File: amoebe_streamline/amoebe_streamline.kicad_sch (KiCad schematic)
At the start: 0 parts

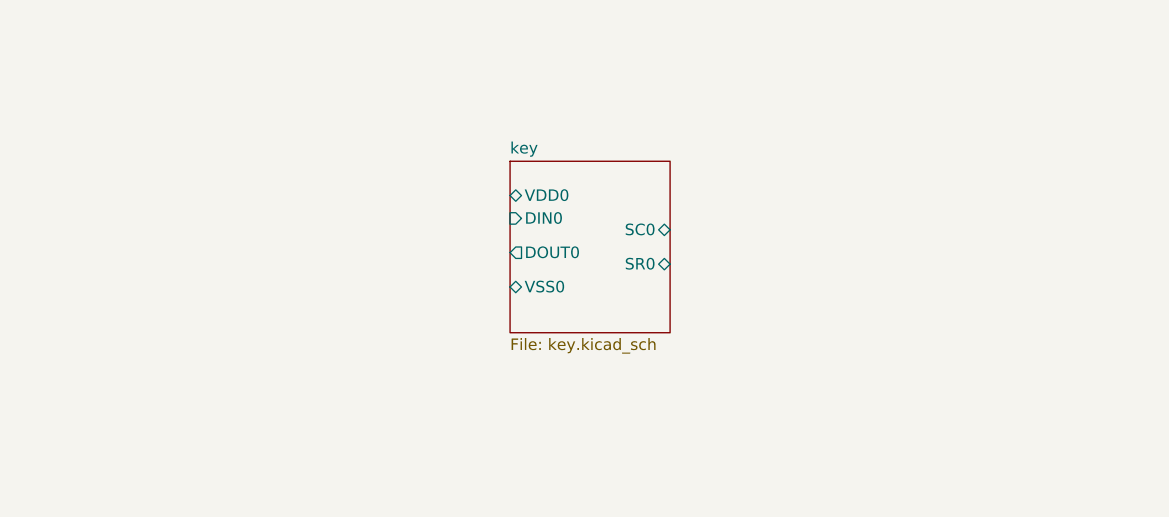
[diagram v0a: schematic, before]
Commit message: Finished schematic and routed traces
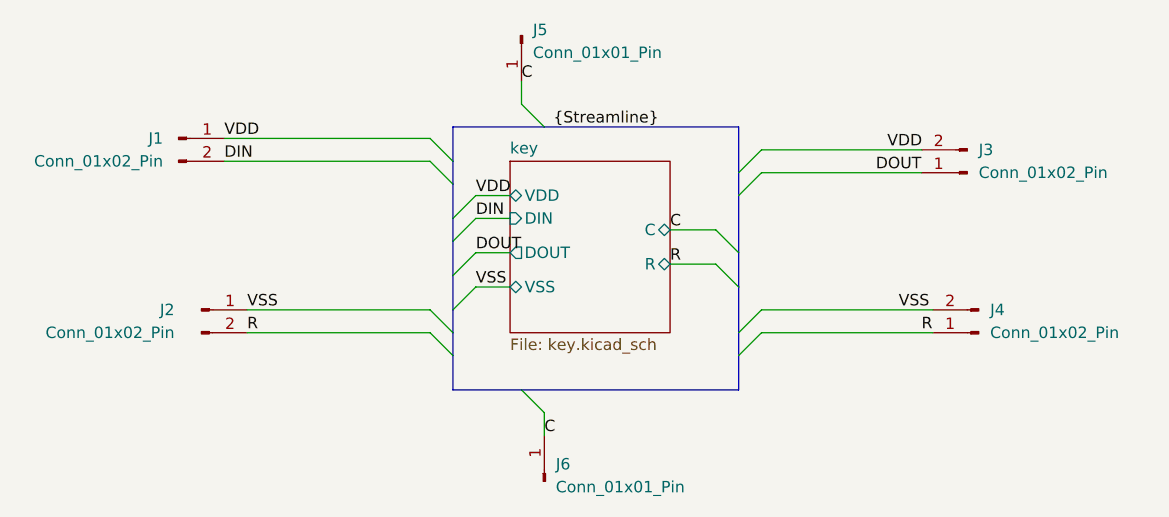
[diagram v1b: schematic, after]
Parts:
- added J1, J2, J3, J4: Conn_01x02_Pin, Connector_Molex:Molex_PicoBlade_53048-0210_1x02_P1.25mm_Horizontal, symbol Connector:Conn_01x02_Pin
- added J5, J6: Conn_01x01_Pin, Connector_PinHeader_1.00mm:PinHeader_1x01_P1.00mm_Horizontal, symbol Connector:Conn_01x01_Pin
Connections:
- new net C: J5.1 (Pin_1), J6.1 (Pin_1)
- new net DIN: J1.2 (Pin_2)
- new net DOUT: J3.1 (Pin_1)
- new net R: J2.2 (Pin_2), J4.1 (Pin_1)
- new net VDD: J1.1 (Pin_1), J3.2 (Pin_2)
- new net VSS: J2.1 (Pin_1), J4.2 (Pin_2)
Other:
- sheet key ports: added C, DIN, DOUT, R, VDD, VSS; removed DIN0, DOUT0, SC0, SR0, VDD0, VSS0

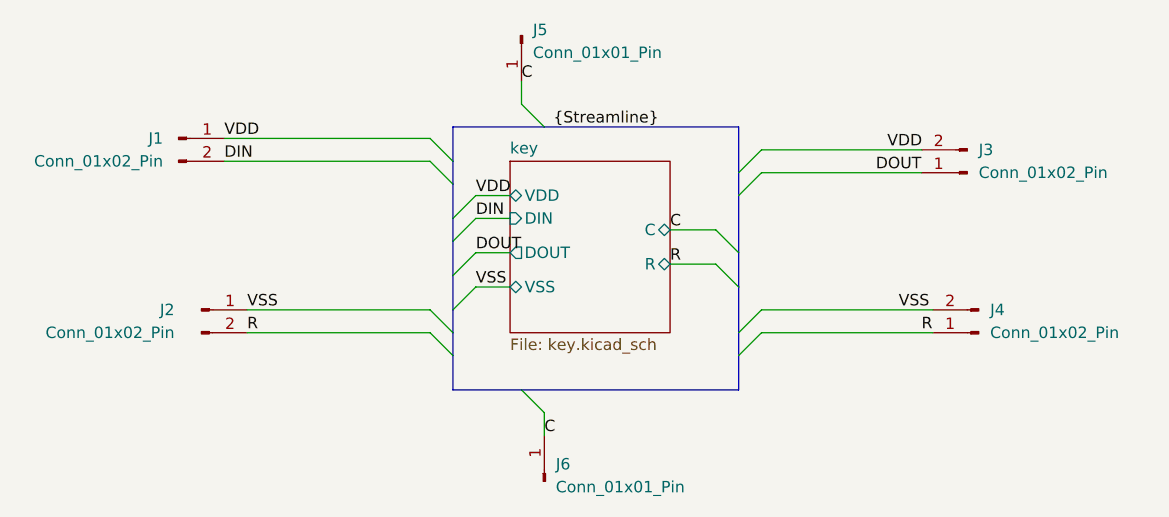
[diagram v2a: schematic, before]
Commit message: version 1.2 with additional ground pins
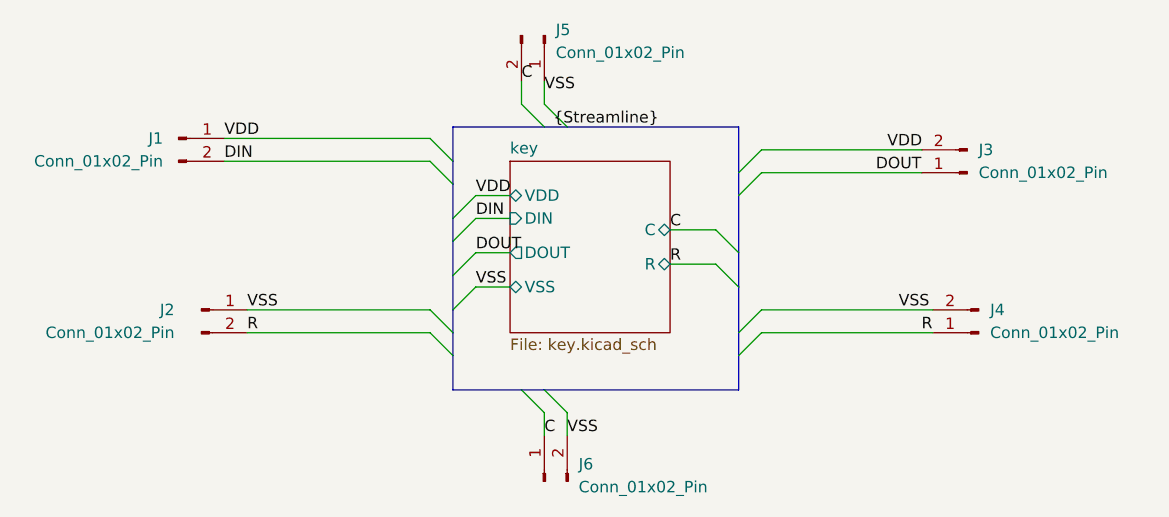
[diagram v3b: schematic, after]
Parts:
- removed J5, J6: Conn_01x01_Pin, Connector_PinHeader_1.00mm:PinHeader_1x01_P1.00mm_Horizontal, symbol Connector:Conn_01x01_Pin
- added J5, J6: Conn_01x02_Pin, Connector_PinHeader_1.00mm:PinHeader_1x02_P1.00mm_Horizontal, symbol Connector:Conn_01x02_Pin
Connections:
- net C: now also J5.2 (Pin_2), J6.1 (Pin_1)
- net VSS: now also J5.1 (Pin_1), J6.2 (Pin_2)
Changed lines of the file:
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@@
 (kicad_sch (version 20230121) (generator eeschema)
   (paper "A4")
-  (bus_alias "Streamline" (members "VDD" "VSS" "R" "C" "DATA"))
+  (bus_alias "Streamline" (members "VDD" "VSS" "R" "C" "DIN" "DOUT"))
   (bus_entry (at 132.08 78.74) (size -2.54 -2.54)
     (stroke (width 0) (type default))
@@
     (stroke (width 0) (type default))
   )
+  (bus_entry (at 144.78 72.39) (size -2.54 -2.54)
+    (stroke (width 0) (type default))
+  )
   (bus_entry (at 132.08 97.79) (size -2.54 -2.54)
     (stroke (width 0) (type default))
@@
     (stroke (width 0) (type default))
   )
+  (bus_entry (at 142.24 101.6) (size 2.54 2.54)
+    (stroke (width 0) (type default))
+  )
   (bus_entry (at 163.83 90.17) (size -2.54 -2.54)
     (stroke (width 0) (type default))
@@
     (stroke (width 0) (type default))
   )
+  (wire (pts (xy 144.78 104.14) (xy 144.78 106.68))
+    (stroke (width 0) (type default))
+  )
   (wire (pts (xy 161.29 87.63) (xy 156.21 87.63))
     (stroke (width 0) (type default))
@@
     (stroke (width 0) (type default))
   )
+  (bus (pts (xy 144.78 72.39) (xy 163.83 72.39))
+    (stroke (width 0) (type default))
+  )
   (bus (pts (xy 163.83 97.79) (xy 163.83 101.6))
     (stroke (width 0) (type default))
@@
     (stroke (width 0) (type default))
   )
+  (wire (pts (xy 142.24 67.31) (xy 142.24 69.85))
+    (stroke (width 0) (type default))
+  )
   (wire (pts (xy 139.7 69.85) (xy 139.7 67.31))
     (stroke (width 0) (type default))
@@
     (stroke (width 0) (type default))
   )
-  (bus (pts (xy 142.24 72.39) (xy 163.83 72.39))
+  (bus (pts (xy 142.24 72.39) (xy 144.78 72.39))
     (stroke (width 0) (type default))
   )
@@
     (stroke (width 0) (type default))
   )
-  (bus (pts (xy 139.7 101.6) (xy 163.83 101.6))
+  (bus (pts (xy 139.7 101.6) (xy 142.24 101.6))
     (stroke (width 0) (type default))
   )
   (bus (pts (xy 132.08 85.09) (xy 132.08 88.9))
+    (stroke (width 0) (type default))
+  )
+  (bus (pts (xy 142.24 101.6) (xy 163.83 101.6))
     (stroke (width 0) (type default))
   )
@@
     (effects (font (size 1.27 1.27)) (justify left bottom))
   )
+  (label "VSS" (at 144.78 106.68 0)
+    (effects (font (size 1.27 1.27)) (justify left bottom))
+  )
   (label "R" (at 156.21 87.63 0) (fields_autoplaced)
+    (effects (font (size 1.27 1.27)) (justify left bottom))
+  )
+  (label "VSS" (at 142.24 68.58 0)
     (effects (font (size 1.27 1.27)) (justify left bottom))
   )
@@
     )
   )
-  (symbol (lib_id "Connector:Conn_01x01_Pin") (at 139.7 62.23 270) (unit 1)
+  (symbol (lib_id "Connector:Conn_01x02_Pin") (at 142.24 111.76 90) (unit 1)
     (in_bom yes) (on_board yes) (dnp no) (fields_autoplaced)
-    (property "Reference" "J5" (at 140.97 61.595 90)
-      (effects (font (size 1.27 1.27)) (justify left))
-    )
-    (property "Value" "Conn_01x01_Pin" (at 140.97 64.135 90)
-      (effects (font (size 1.27 1.27)) (justify left))
-    )
-    (property "Footprint" "Connector_PinHeader_1.00mm:PinHeader_1x01_P1.00mm_Horizontal" (at 139.7 62.23 0)
-      (effects (font (size 1.27 1.27)) hide)
-    )
-    (property "Datasheet" "~" (at 139.7 62.23 0)
-      (effects (font (size 1.27 1.27)) hide)
-    )
-    (pin "1")
-    (instances
-      (project "amoebe_streamline"
-        (path "/f7434787-4d52-45e0-bcf8-72783deb577d"
-          (reference "J5") (unit 1)
-        )
-      )
-    )
-  )
-  (symbol (lib_id "Connector:Conn_01x01_Pin") (at 142.24 111.76 90) (unit 1)
-    (in_bom yes) (on_board yes) (dnp no) (fields_autoplaced)
-    (property "Reference" "J6" (at 143.51 109.855 90)
-      (effects (font (size 1.27 1.27)) (justify right))
-    )
-    (property "Value" "Conn_01x01_Pin" (at 143.51 112.395 90)
-      (effects (font (size 1.27 1.27)) (justify right))
-    )
-    (property "Footprint" "Connector_PinHeader_1.00mm:PinHeader_1x01_P1.00mm_Horizontal" (at 142.24 111.76 0)
+    (property "Reference" "J6" (at 146.05 109.855 90)
+      (effects (font (size 1.27 1.27)) (justify right))
+    )
+    (property "Value" "Conn_01x02_Pin" (at 146.05 112.395 90)
+      (effects (font (size 1.27 1.27)) (justify right))
+    )
+    (property "Footprint" "Connector_PinHeader_1.00mm:PinHeader_1x02_P1.00mm_Horizontal" (at 142.24 111.76 0)
       (effects (font (size 1.27 1.27)) hide)
     )
@@
       (effects (font (size 1.27 1.27)) hide)
     )
+    (pin "2")
     (pin "1")
     (instances
@@
         )
       )
+    )
+  )
+  (symbol (lib_id "Connector:Conn_01x02_Pin") (at 142.24 62.23 270) (unit 1)
+    (in_bom yes) (on_board yes) (dnp no) (fields_autoplaced)
+    (property "Reference" "J5" (at 143.51 61.595 90)
+      (effects (font (size 1.27 1.27)) (justify left))
+    )
+    (property "Value" "Conn_01x02_Pin" (at 143.51 64.135 90)
+      (effects (font (size 1.27 1.27)) (justify left))
+    )
+    (property "Footprint" "Connector_PinHeader_1.00mm:PinHeader_1x02_P1.00mm_Horizontal" (at 142.24 62.23 0)
+      (effects (font (size 1.27 1.27)) hide)
+    )
+    (property "Datasheet" "~" (at 142.24 62.23 0)
+      (effects (font (size 1.27 1.27)) hide)
+    )
+    (pin "2")
+    (pin "1")
+    (instances
+      (project "amoebe_streamline"
+        (path "/f7434787-4d52-45e0-bcf8-72783deb577d"
+          (reference "J5") (unit 1)
+        )
+      )

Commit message: updated pcb design
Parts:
- J1, J2, J3, J4: footprint Connector_Molex:Molex_PicoBlade_53048-0210_1x02_P1.25mm_Horizontal -> Connector_Molex:Molex_PicoBlade_53047-0210_1x02_P1.25mm_Vertical
- J5, J6: footprint Connector_PinHeader_1.00mm:PinHeader_1x02_P1.00mm_Horizontal -> Connector_Molex:Molex_PicoBlade_53047-0210_1x02_P1.25mm_Vertical
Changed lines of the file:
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@@
     (effects (font (size 1.27 1.27)) (justify left bottom))
   )
-  (label "VSS" (at 144.78 106.68 0)
+  (label "VSS" (at 144.78 106.68 0) (fields_autoplaced)
     (effects (font (size 1.27 1.27)) (justify left bottom))
   )
@@
     (effects (font (size 1.27 1.27)) (justify left bottom))
   )
-  (label "VSS" (at 142.24 68.58 0)
+  (label "VSS" (at 142.24 68.58 0) (fields_autoplaced)
     (effects (font (size 1.27 1.27)) (justify left bottom))
   )
@@
       (effects (font (size 1.27 1.27)))
     )
-    (property "Footprint" "Connector_Molex:Molex_PicoBlade_53048-0210_1x02_P1.25mm_Horizontal" (at 101.6 73.66 0)
+    (property "Footprint" "Connector_Molex:Molex_PicoBlade_53047-0210_1x02_P1.25mm_Vertical" (at 101.6 73.66 0)
       (effects (font (size 1.27 1.27)) hide)
     )
@@
       (effects (font (size 1.27 1.27)) (justify right))
     )
-    (property "Footprint" "Connector_Molex:Molex_PicoBlade_53048-0210_1x02_P1.25mm_Horizontal" (at 190.5 95.25 0)
+    (property "Footprint" "Connector_Molex:Molex_PicoBlade_53047-0210_1x02_P1.25mm_Vertical" (at 190.5 95.25 0)
       (effects (font (size 1.27 1.27)) hide)
     )
@@
       (effects (font (size 1.27 1.27)) (justify right))
     )
-    (property "Footprint" "Connector_PinHeader_1.00mm:PinHeader_1x02_P1.00mm_Horizontal" (at 142.24 111.76 0)
+    (property "Footprint" "Connector_Molex:Molex_PicoBlade_53047-0210_1x02_P1.25mm_Vertical" (at 142.24 111.76 0)
       (effects (font (size 1.27 1.27)) hide)
     )
@@
       (effects (font (size 1.27 1.27)) hide)
     )
+    (pin "1")
     (pin "2")
-    (pin "1")
     (instances
       (project "amoebe_streamline"
@@
       (effects (font (size 1.27 1.27)) (justify right))
     )
-    (property "Footprint" "Connector_Molex:Molex_PicoBlade_53048-0210_1x02_P1.25mm_Horizontal" (at 189.23 77.47 0)
+    (property "Footprint" "Connector_Molex:Molex_PicoBlade_53047-0210_1x02_P1.25mm_Vertical" (at 189.23 77.47 0)
       (effects (font (size 1.27 1.27)) hide)
     )
@@
       (effects (font (size 1.27 1.27)) (justify left))
     )
-    (property "Footprint" "Connector_PinHeader_1.00mm:PinHeader_1x02_P1.00mm_Horizontal" (at 142.24 62.23 0)
+    (property "Footprint" "Connector_Molex:Molex_PicoBlade_53047-0210_1x02_P1.25mm_Vertical" (at 142.24 62.23 0)
       (effects (font (size 1.27 1.27)) hide)
     )
@@
       (effects (font (size 1.27 1.27)) hide)
     )
+    (pin "1")
     (pin "2")
-    (pin "1")
     (instances
       (project "amoebe_streamline"
@@
       (effects (font (size 1.27 1.27)))
     )
-    (property "Footprint" "Connector_Molex:Molex_PicoBlade_53048-0210_1x02_P1.25mm_Horizontal" (at 104.14 92.71 0)
+    (property "Footprint" "Connector_Molex:Molex_PicoBlade_53047-0210_1x02_P1.25mm_Vertical" (at 104.14 92.71 0)
       (effects (font (size 1.27 1.27)) hide)
     )
